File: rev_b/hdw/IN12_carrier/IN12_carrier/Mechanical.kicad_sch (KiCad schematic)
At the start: 8 parts

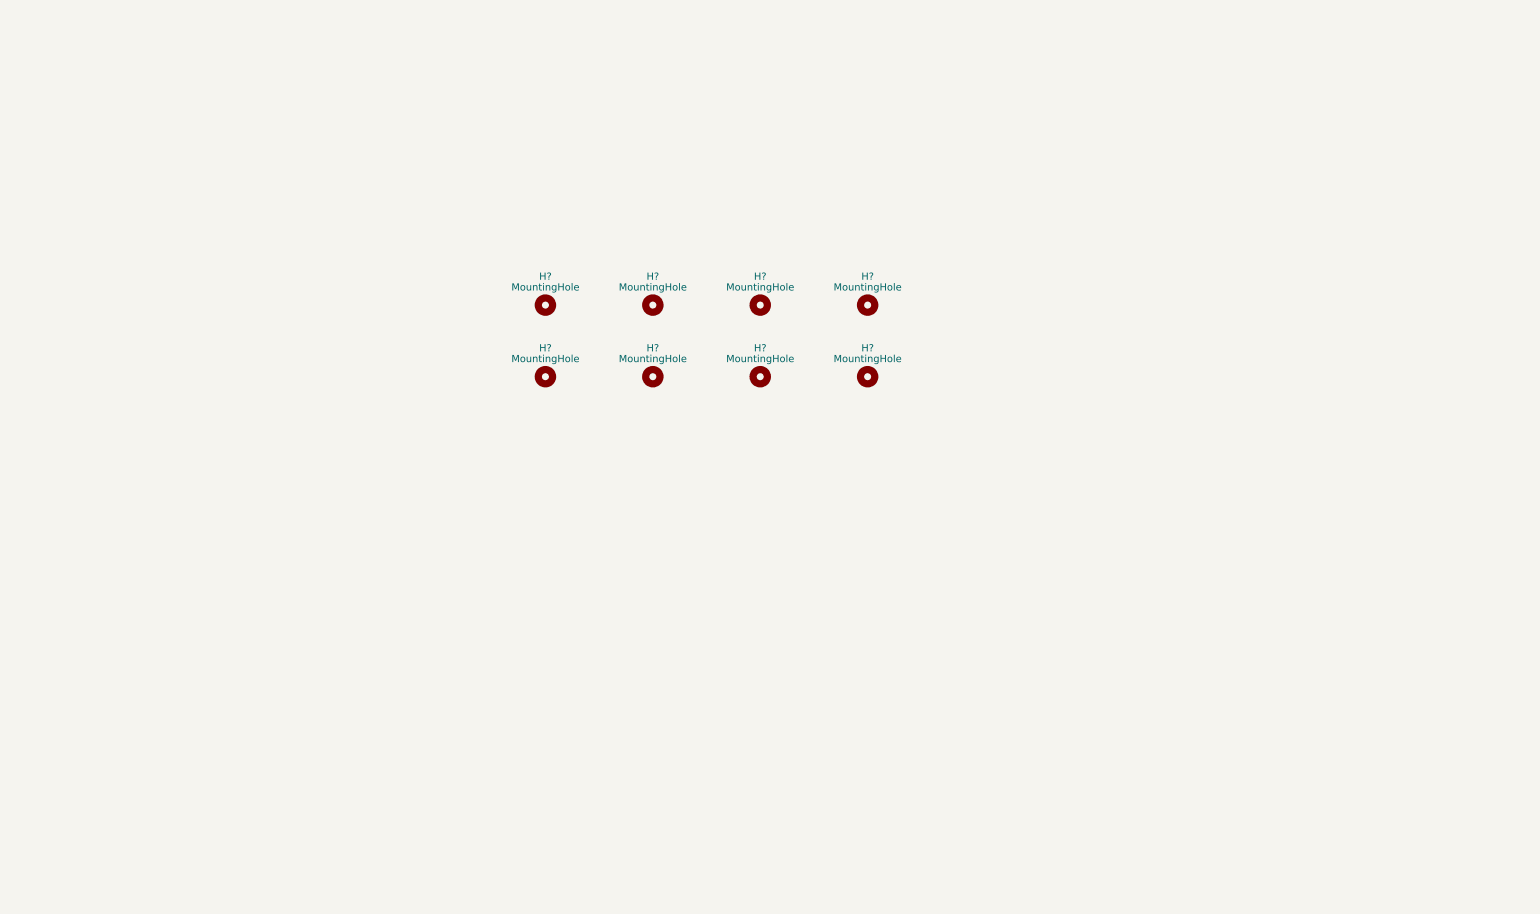
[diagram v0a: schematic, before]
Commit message: added BOM for IN12 carrier, finished routing, some schematic tweaks, adjusted design rules for ERC
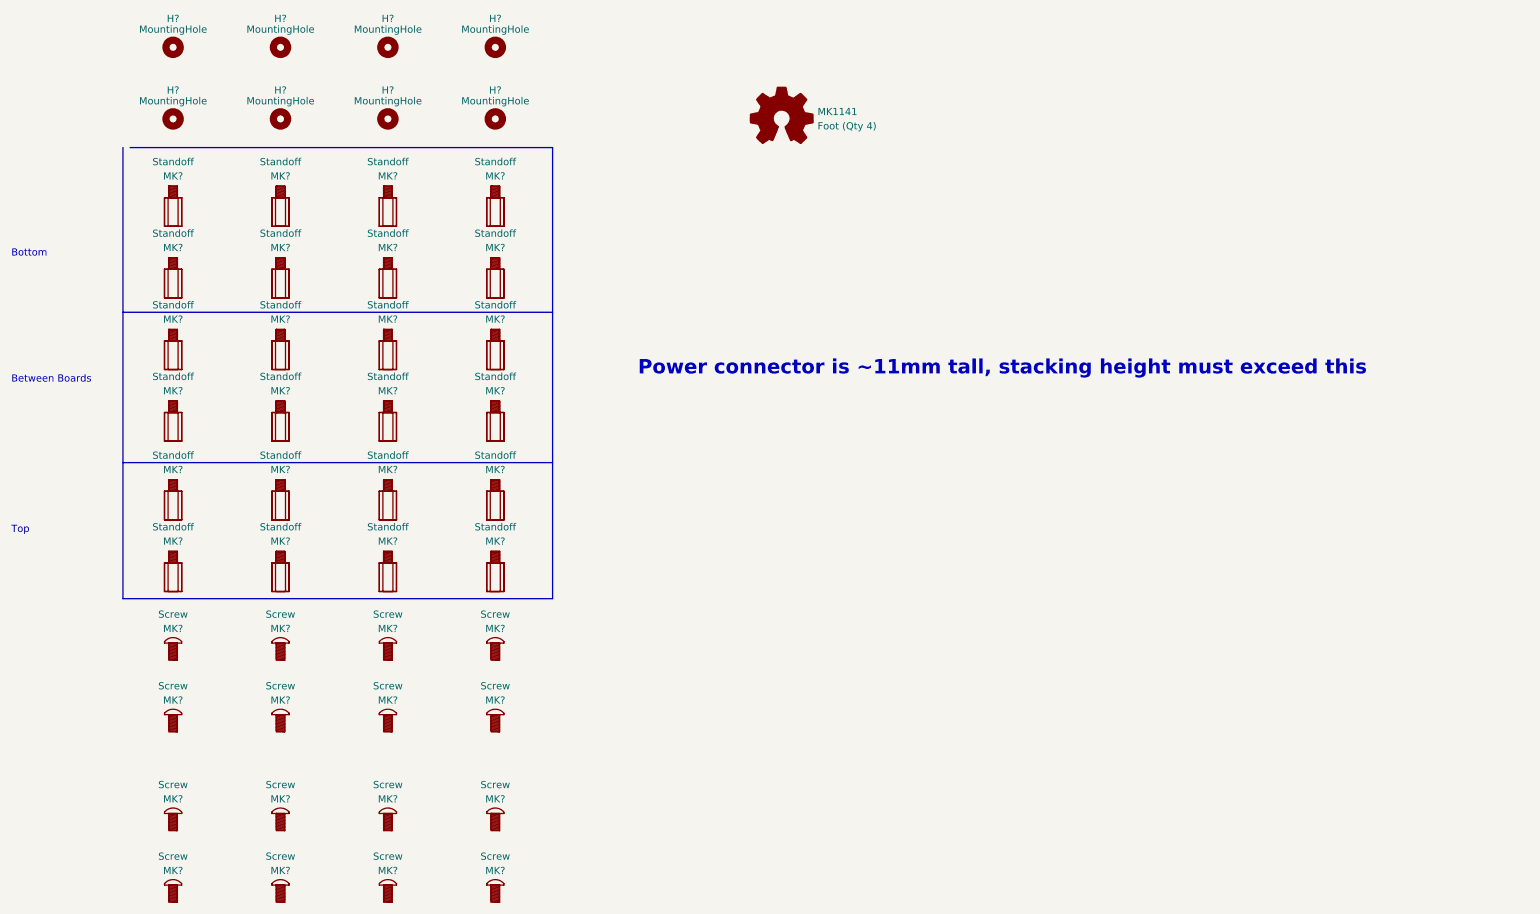
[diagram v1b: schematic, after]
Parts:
- added MK1141: Foot (Qty 4), symbol Graphic:Logo_Open_Hardware_Small
- added MK? (x24): Standoff, symbol Custom_Library:Standoff
- added MK? (x16): Screw, symbol Custom_Library:Screw
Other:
- note added: "Between Boards"
- note added: "Bottom"
- note added: "Power connector is ~11mm tall, stacking height must exceed this"
- note added: "Top"
- moved on the sheet: H?
